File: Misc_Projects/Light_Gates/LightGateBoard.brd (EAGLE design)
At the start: 30.5 x 63.5 mm, 17 parts, among them T1 PHOTOTRANSISTOR

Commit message: Added changes to LightGateBoard
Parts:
- removed R3: 4.7k, 1-Passive Components:1/4W-0.3
- removed T1: PHOTOTRANSISTOR, 1-Active Components:LED-5MM
- added JP5, JP6: (no value), GTOR - Connectors:1X01
- added PH1: PHOTORESISTOR0N1, GTOR - Passive Components:TO46-VT200
- added R6: (no value), GTOR - Passive Components:3RP/1610N
- moved JP2 21.2 mm to (32.1, 37.6)
- moved IC1 9.91 mm to (27.6, 47.2)
- moved LED2 8.89 mm to (21.6, 54.6)
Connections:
- net 3V3: now also PH1.1; no longer R3.2
- net GND: now also R6.1; no longer T1.K
- net SIG: now also JP5.1, JP6.1, PH1.2, R6.2; no longer R3.1, T1.A
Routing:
- net 5V: track 39.4 -> 70.4 mm
- net GND: track 147.5 -> 171.1 mm
- net 3V3: track 66.2 -> 83.7 mm
- net SIG_START: track 15.1 -> 0.00 mm
- net VCC: track 93.5 -> 102.9 mm
- net SIG: track 103.7 -> 111.5 mm
- net N$7: track 6.89 -> 0.00 mm
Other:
- board size 30.5 x 63.5 mm -> 41.9 x 63.5 mm

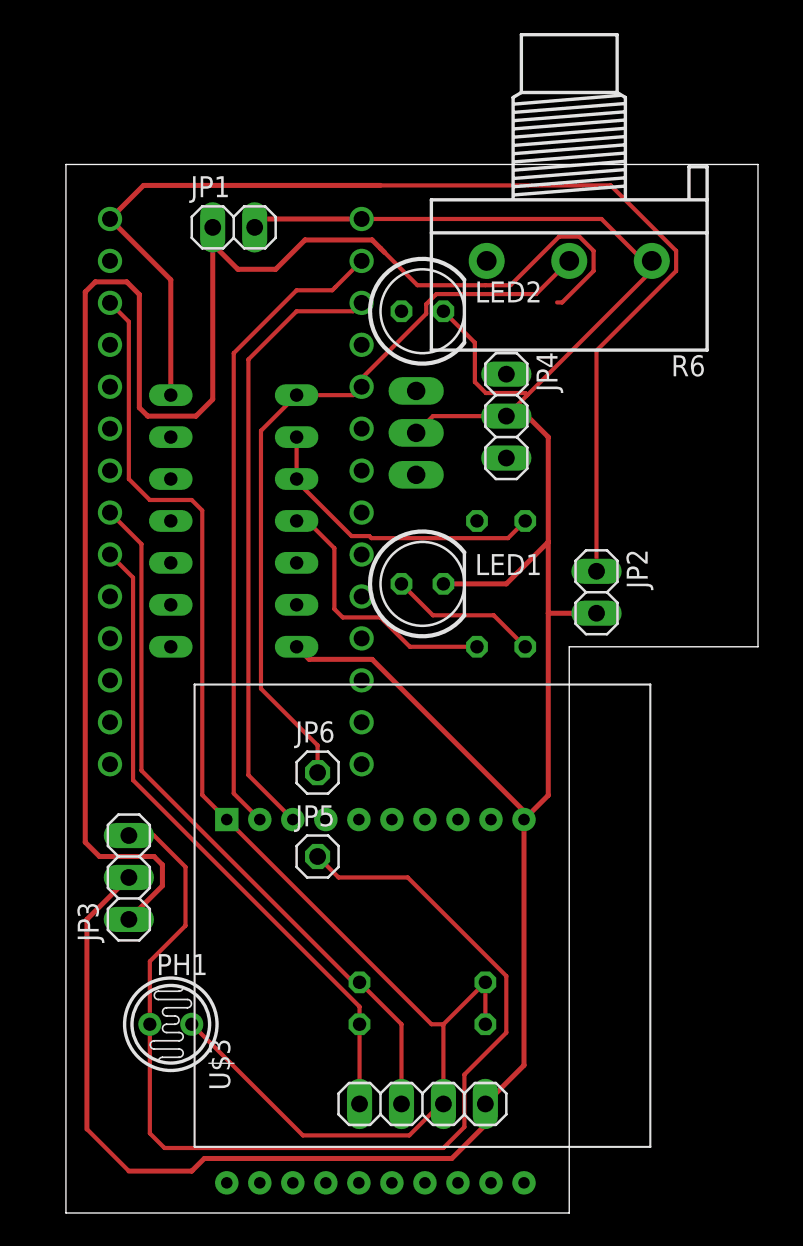
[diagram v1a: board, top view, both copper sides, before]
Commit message: Redid PCB with bigger traces and changed photodiode to photoresistor
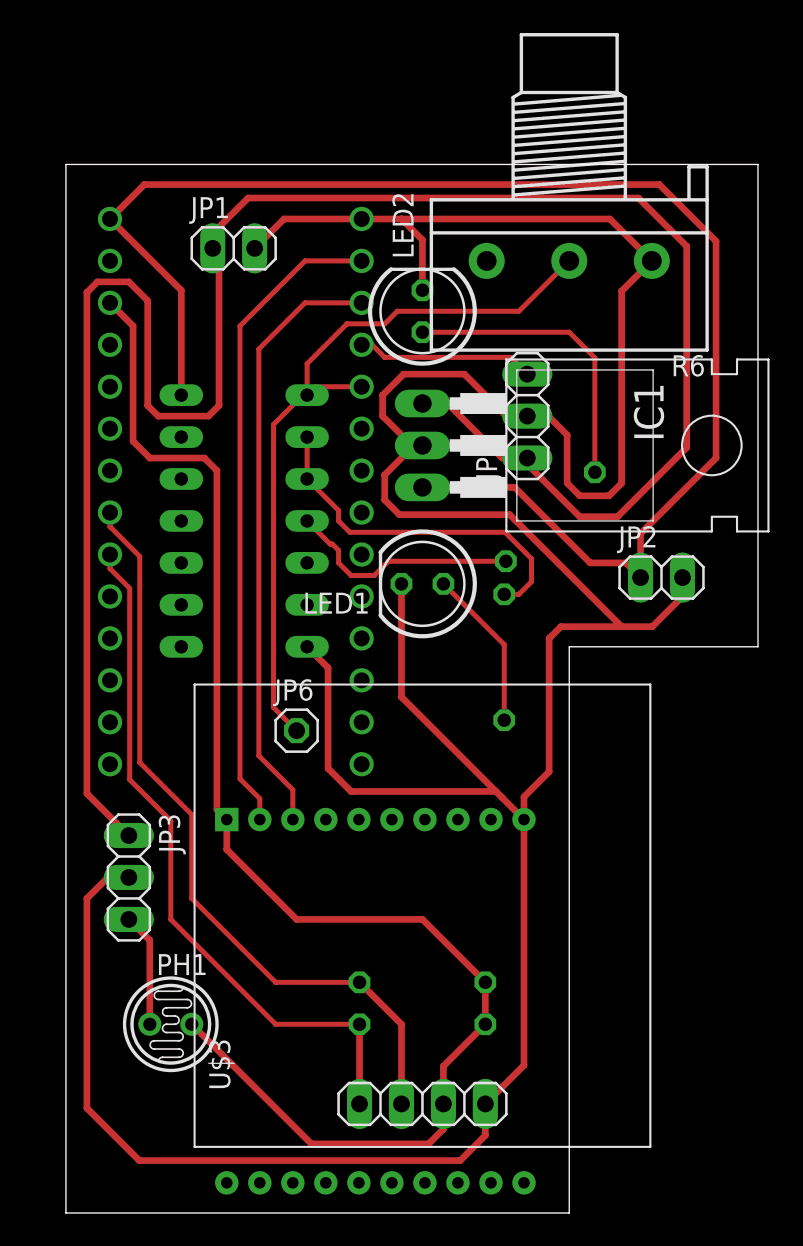
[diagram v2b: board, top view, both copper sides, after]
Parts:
- removed JP5: (no value), GTOR - Connectors:1X01
- moved R5 6.02 mm to (29.3, 42.2), turned to 135 degrees
- moved R4 4.62 mm to (26.5, 33.7)
- moved JP2 4.04 mm to (36.1, 38.5), turned to 0 degrees
- moved JP6 2.84 mm to (14.0, 29.2)
- moved JP4 1.27 mm to (27.9, 48.3), turned to 90 degrees
- moved JP1 1.27 mm to (10.2, 58.4)
- moved IC1 0.85 mm to (27.9, 46.5), flipped to the top, turned to 270 degrees
- moved V1 0.63 mm to (10.8, 41.9)
- turned JP3 to 270 degrees
- turned LED1 to 180 degrees
- turned LED2 to 90 degrees
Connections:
- net SIG: no longer JP5.1
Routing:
- net SIG: track 111.5 -> 52.6 mm
- net GND: track 171.1 -> 211.3 mm
- net VCC: track 102.9 -> 123.9 mm
- net 5V: track 70.4 -> 89.2 mm
- net N$7: track 0.00 -> 18.0 mm
- net SIG_START: track 0.00 -> 10.8 mm
- net NSIG: track 18.4 -> 21.9 mm
- net SDA: track 39.5 -> 42.5 mm
- net SCL: track 43.3 -> 46.1 mm
- net N$6: track 16.2 -> 14.2 mm
- net 3V3: track 83.7 -> 85.5 mm
- net N$1: track 9.07 -> 9.78 mm
- net TX: track 37.3 -> 36.7 mm

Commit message: Fixed signal on PCB's, ready for manufacturing
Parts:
- removed JP6: (no value), GTOR - Connectors:1X01
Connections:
- removed net N$6: R5.1, V1.4
- new net SIG_END: JP3.3, R5.1, U$1.3/CANTX, V1.4
- net SIG: no longer JP3.3, JP6.1, U$1.3/CANTX
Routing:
- net SIG_END: track 0.00 -> 68.8 mm
- net N$6: track 14.2 -> 0.00 mm
- net SIG: track 52.6 -> 62.4 mm
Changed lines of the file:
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@@
 <attribute name="VALUE" x="33.655" y="55.118" size="1.27" layer="27" rot="R180"/>
-</element>
-<element name="JP6" library="GTOR - Connectors" package="1X01" package3d_urn="urn:adsk.eagle:package:22485/2" value="" x="13.97" y="29.21" smashed="yes">
-<attribute name="NAME" x="12.6238" y="31.0388" size="1.27" layer="25" ratio="10"/>
-<attribute name="POPULARITY" value="64" x="13.97" y="29.21" size="1.778" layer="27" display="off"/>
-<attribute name="VALUE" x="12.7" y="26.035" size="1.27" layer="27"/>
 </element>
 </elements>
@@
 </signal>
 <signal name="SIG">
-<contactref element="JP3" pad="3"/>
 <contactref element="V1" pad="1"/>
-<contactref element="U$1" pad="3/CANTX"/>
 <contactref element="PH1" pad="2"/>
 <contactref element="R6" pad="2"/>
-<contactref element="JP6" pad="1"/>
-<wire x1="3.81" y1="17.78" x2="5.08" y2="16.51" width="0.4064" layer="1"/>
-<wire x1="5.08" y1="16.51" x2="5.08" y2="11.43" width="0.4064" layer="1"/>
-<wire x1="13.97" y1="29.21" x2="12.573" y2="30.607" width="0.3048" layer="1"/>
-<wire x1="14.351" y1="49.53" x2="14.605" y2="49.53" width="0.3048" layer="1"/>
-<wire x1="12.573" y1="30.607" x2="12.573" y2="47.752" width="0.3048" layer="1"/>
-<wire x1="12.573" y1="47.752" x2="14.351" y2="49.53" width="0.3048" layer="1"/>
-<wire x1="14.605" y1="49.53" x2="15.113" y2="50.038" width="0.3048" layer="1"/>
-<wire x1="15.113" y1="50.038" x2="17.907" y2="50.038" width="0.3048" layer="1"/>
 <wire x1="30.48" y1="57.658" x2="27.432" y2="54.61" width="0.3048" layer="1"/>
 <wire x1="19.304" y1="53.848" x2="17.018" y2="53.848" width="0.3048" layer="1"/>
@@
 <wire x1="27.432" y1="54.61" x2="20.066" y2="54.61" width="0.3048" layer="1"/>
 <wire x1="20.066" y1="54.61" x2="19.304" y2="53.848" width="0.3048" layer="1"/>
-<wire x1="3.81" y1="17.78" x2="13.97" y2="29.21" width="0" layer="19" extent="1-1"/>
+<wire x1="5.08" y1="11.43" x2="7.62" y2="13.97" width="0.3048" layer="16"/>
+<wire x1="7.62" y1="27.94" x2="11.43" y2="31.75" width="0.3048" layer="16"/>
+<wire x1="11.43" y1="46.355" x2="14.605" y2="49.53" width="0.3048" layer="16"/>
+<wire x1="7.62" y1="13.97" x2="7.62" y2="27.94" width="0.3048" layer="16"/>
+<wire x1="11.43" y1="31.75" x2="11.43" y2="46.355" width="0.3048" layer="16"/>
 </signal>
 <signal name="SDA">
@@
 <wire x1="28.194" y1="38.227" x2="27.432" y2="37.465" width="0.3048" layer="1"/>
 </signal>
-<signal name="N$6">
+<signal name="SIG_END">
 <contactref element="V1" pad="4"/>
 <contactref element="R5" pad="1"/>
@@
 <wire x1="17.272" y1="38.608" x2="18.669" y2="38.608" width="0.3048" layer="1"/>
 <wire x1="18.669" y1="38.608" x2="19.530921875" y2="39.469921875" width="0.3048" layer="1"/>
+<contactref element="U$1" pad="3/CANTX"/>
+<contactref element="JP3" pad="3"/>
+<wire x1="3.81" y1="17.78" x2="6.35" y2="20.32" width="0.3048" layer="16"/>
+<wire x1="10.16" y1="33.02" x2="10.16" y2="50.8" width="0.3048" layer="16"/>
+<wire x1="10.16" y1="50.8" x2="11.43" y2="52.07" width="0.3048" layer="16"/>
+<wire x1="15.875" y1="52.07" x2="17.907" y2="50.038" width="0.3048" layer="16"/>
+<wire x1="6.35" y1="20.32" x2="6.35" y2="29.21" width="0.3048" layer="16"/>
+<wire x1="6.35" y1="29.21" x2="10.16" y2="33.02" width="0.3048" layer="16"/>
+<wire x1="11.43" y1="52.07" x2="15.875" y2="52.07" width="0.3048" layer="16"/>
+<wire x1="17.907" y1="50.038" x2="16.51" y2="48.641" width="0.3048" layer="16"/>
+<wire x1="16.51" y1="43.18" x2="15.24" y2="41.91" width="0.3048" layer="16"/>
+<wire x1="15.24" y1="41.91" x2="14.605" y2="41.91" width="0.3048" layer="16"/>
+<wire x1="16.51" y1="48.641" x2="16.51" y2="43.18" width="0.3048" layer="16"/>
 </signal>
 <signal name="N$7">
@@
 <mfgpreviewcolor name="substratecolor" color="0xFF786E46"/>
 </mfgpreviewcolors>
-<errors>
-</errors>
 </board>
 </drawing>
